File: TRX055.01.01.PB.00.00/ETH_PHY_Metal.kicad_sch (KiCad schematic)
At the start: 1 part, among them U11 KSZ9031RNXCA

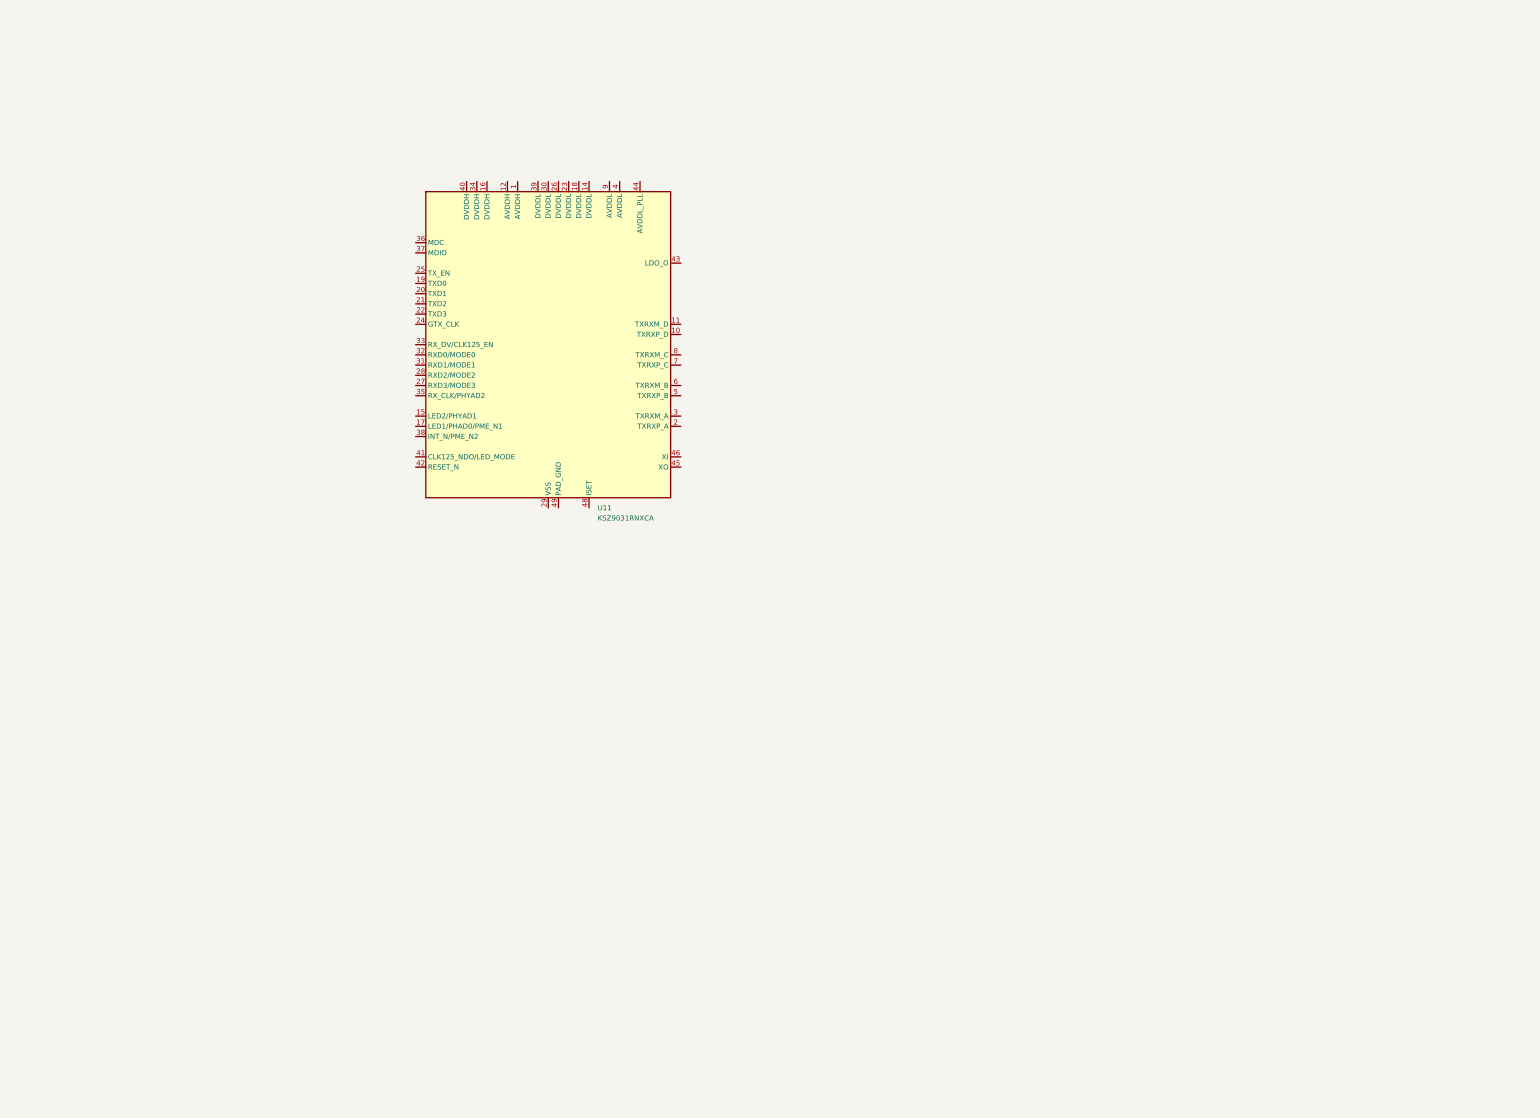
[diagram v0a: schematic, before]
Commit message: +ETH +USB +Connectors
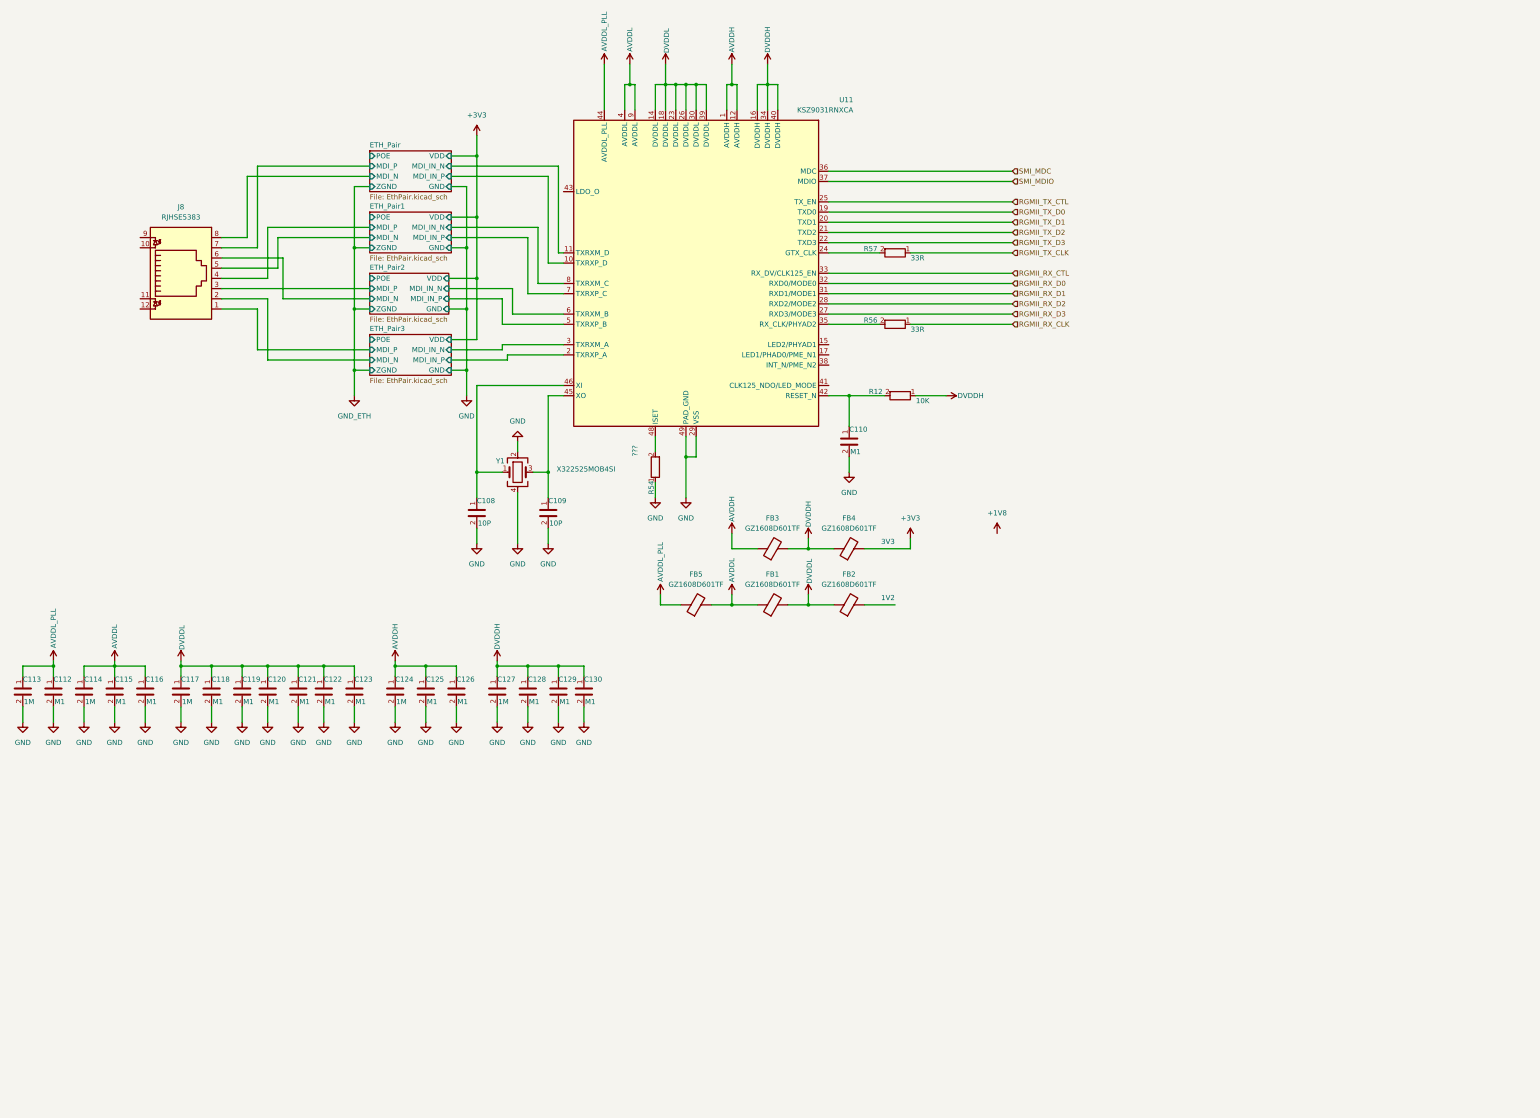
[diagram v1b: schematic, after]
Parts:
- added C108, C109: 10P, Capacitor_SMD:C_0402_1005Metric, symbol PPA-Pasive:Cap
- added C110, C112, C115, C116, C118, C119, C120, C121, C122, C123, C125, C126, C128, C129, C130: M1, Capacitor_SMD:C_0402_1005Metric, symbol PPA-Pasive:Cap
- added C113, C114, C117, C124, C127: 1M, Capacitor_SMD:C_0402_1005Metric, symbol PPA-Pasive:Cap
- added FB1, FB2, FB3, FB4, FB5: GZ1608D601TF, Inductor_SMD:L_0603_1608Metric, symbol Device:FerriteBead
- added J8: RJHSE5383, Connector_RJ:RJ45_Amphenol_RJHSE538X, symbol Connector:RJ45_LED
- added R12: 10K, Resistor_SMD:R_0402_1005Metric, symbol PPA-Pasive:Res
- added R54: ???, Resistor_SMD:R_0402_1005Metric, symbol PPA-Pasive:Res
- added R56, R57: 33R, Resistor_SMD:R_0402_1005Metric, symbol PPA-Pasive:Res
- added Y1: X322525MOB4SI, Crystal:Crystal_SMD_3225-4Pin_3.2x2.5mm, symbol Device:Crystal_GND24
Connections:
- net AVDDH: now reaches U11.1 (AVDDH)
- net AVDDH: now also U11.12 (AVDDH), C124.1, C125.1, C126.1, FB3.1
- net ETH_Pair/MDI_IN_P: now reaches U11.10 (TXRXP_D)
- net ETH_Pair/MDI_IN_N: now reaches U11.11 (TXRXM_D)
- net DVDDL: now reaches U11.14 (DVDDL)
- net DVDDL: now also U11.18 (DVDDL), U11.23 (DVDDL), U11.26 (DVDDL), U11.30 (DVDDL), U11.39 (DVDDL), C117.1, C118.1, C119.1, C120.1, C121.1, C122.1, C123.1, FB1.2, FB2.1
- net DVDDH: now reaches U11.16 (DVDDH)
- net DVDDH: now also U11.34 (DVDDH), U11.40 (DVDDH), C127.1, C128.1, C129.1, C130.1, FB3.2, FB4.1, R12.1
- net RGMII_TX_D0: now reaches U11.19 (TXD0)
- net ETH_Pair3/MDI_IN_P: now reaches U11.2 (TXRXP_A)
- net RGMII_TX_D1: now reaches U11.20 (TXD1)
- net RGMII_TX_D2: now reaches U11.21 (TXD2)
- net RGMII_TX_D3: now reaches U11.22 (TXD3)
- net at U11.24 (GTX_CLK): now also R57.2
- net RGMII_TX_CTL: now reaches U11.25 (TX_EN)
- net RGMII_RX_D3: now reaches U11.27 (RXD3/MODE3)
- net RGMII_RX_D2: now reaches U11.28 (RXD2/MODE2)
- net GND: now reaches U11.29 (VSS)
- net GND: now also U11.49 (PAD_GND), C108.2, C109.2, C110.2, C112.2, C113.2, C114.2, C115.2, C116.2, C117.2, C118.2, C119.2, C120.2, C121.2, C122.2, C123.2, C124.2, C125.2, C126.2, C127.2, C128.2, C129.2, C130.2, R54.1, Y1.2, Y1.4
- net ETH_Pair3/MDI_IN_N: now reaches U11.3 (TXRXM_A)
- net RGMII_RX_D1: now reaches U11.31 (RXD1/MODE1)
- net RGMII_RX_D0: now reaches U11.32 (RXD0/MODE0)
- net RGMII_RX_CTL: now reaches U11.33 (RX_DV/CLK125_EN)
- net at U11.35 (RX_CLK/PHYAD2): now also R56.2
- net SMI_MDC: now reaches U11.36 (MDC)
- net SMI_MDIO: now reaches U11.37 (MDIO)
- net AVDDL: now reaches U11.4 (AVDDL)
- net AVDDL: now also U11.9 (AVDDL), C114.1, C115.1, C116.1, FB1.1, FB5.2
- net at U11.42 (RESET_N): now also C110.1, R12.2
- net AVDDL_PLL: now reaches U11.44 (AVDDL_PLL)
- net AVDDL_PLL: now also C112.1, C113.1, FB5.1
- net at U11.45 (XO): now also C109.1, Y1.3
- net at U11.46 (XI): now also C108.1, Y1.1
- net at U11.48 (ISET): now also R54.2
- net ETH_Pair2/MDI_IN_P: now reaches U11.5 (TXRXP_B)
- net ETH_Pair2/MDI_IN_N: now reaches U11.6 (TXRXM_B)
- net ETH_Pair1/MDI_IN_P: now reaches U11.7 (TXRXP_C)
- net ETH_Pair1/MDI_IN_N: now reaches U11.8 (TXRXM_C)
- new net +3V3: FB4.2
- new net ETH_Pair/MDI_N: J8.8
- new net ETH_Pair/MDI_P: J8.7
- new net ETH_Pair1/MDI_N: J8.5
- new net ETH_Pair1/MDI_P: J8.4
- new net ETH_Pair2/MDI_N: J8.6
- new net ETH_Pair2/MDI_P: J8.3
- new net ETH_Pair3/MDI_N: J8.2
- new net ETH_Pair3/MDI_P: J8.1
- new net RGMII_RX_CLK: R56.1
- new net RGMII_TX_CLK: R57.1
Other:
- added sheet ETH_Pair (EthPair.kicad_sch)
- added sheet ETH_Pair1 (EthPair.kicad_sch)
- added sheet ETH_Pair2 (EthPair.kicad_sch)
- added sheet ETH_Pair3 (EthPair.kicad_sch)
- note added: "1V2"
- note added: "3V3"
- moved on the sheet: U11

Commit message: + add clocks + add PSU
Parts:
- C108, C109: JLCPCB Part # (none) -> C25744; Voltage 6V3 -> 100V
- C110, C112, C115, C116, C118, C119, C120, C121, C122, C123, C125, C126, C128, C129, C130: footprint Capacitor_SMD:C_0402_1005Metric -> Capacitor_SMD:C_0201_0603Metric; JLCPCB Part # (none) -> C1581; Voltage 6V3 -> 100V
- C113, C114, C117, C124, C127: JLCPCB Part # (none) -> C52923; Voltage 6V3 -> 100V
- FB1, FB2, FB3, FB4, FB5: value GZ1608D601TF -> BLM18PG330SN1D; JLCPCB Part # C1002 -> C88984
- R12: JLCPCB Part # (none) -> C25744
- R54: value ??? -> 12K1; JLCPCB Part # (none) -> C132157
- R56, R57: JLCPCB Part # (none) -> C25105
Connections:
- net +1V8: now also C127.1, C128.1, C129.1, C130.1, R12.1, U11.16 (DVDDH), U11.34 (DVDDH), U11.40 (DVDDH)
- removed net DVDDH: C127.1, C128.1, C129.1, C130.1, FB3.2, FB4.1, R12.1, U11.16 (DVDDH), U11.34 (DVDDH), U11.40 (DVDDH)
- new net: FB3.2, FB4.1

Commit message: V0.1 - production, added brig-up comments
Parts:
- added C178: M1, Capacitor_SMD:C_0201_0603Metric, symbol PPA-Pasive:Cap
- added C288, C324, C325, C326: 10M, Capacitor_SMD:C_0603_1608Metric, symbol PPA-Pasive:Cap
- added C289: 1M, Capacitor_SMD:C_0402_1005Metric, symbol PPA-Pasive:Cap
- added R107, R108, R160, R161: 10K, Resistor_SMD:R_0402_1005Metric, symbol PPA-Pasive:Res
- added U31: NCP186AMN080TBG, ppa-active:DFN-12_L4.0-W4.0-P0.65-BL-EP3.4, symbol ppa-ic-power:NCP186AMN080TBG
- C110: value M1 -> 10M
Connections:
- net +3V3: now also C288.1, U31.10 (IN), U31.11 (IN), U31.9 (EN)
- net AVDDH: now also C325.1
- net GND: now also C178.2, C288.2, C289.2, C324.2, C325.2, C326.2, R108.2, U31.13 (EP), U31.8 (GND)
- net VDD_DVDDL: now reaches FB2.2
- net VDD_DVDDL: now also C289.1, R107.1, U31.2 (OUT), U31.3 (OUT)
- net VDD_PORT: now reaches FB3.2, FB4.1
- net VDD_PORT: now also C178.1, C324.1, C326.1, R160.1, R161.1
- net nLED2: now reaches U11.15 (LED2/PHYAD1)
- net nLED2: now also J8.9
- net nLED1: now reaches U11.17 (LED1/PHAD0/PME_N1)
- net nLED1: now also J8.11
- net at J8.10: now also R161.2
- net at J8.12: now also R160.2
- new net: R107.2, R108.1, U31.5 (FB/ADJ)
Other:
- note added: "TBD: Measure magnetics compliance"
- note added: "TBD: port protection"
- company: (none) -> Tronex s.r.o. / Tronex Group USA LLC
- title: (none) -> TRNX SDR Carrier board
- moved on the sheet: C108, C109, C110, C112, C113, C114, C115, C116, C117, C118, C119, C120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
